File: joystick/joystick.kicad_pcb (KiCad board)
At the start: 2 copper layers, 33 x 34.3 mm, 2 parts, among them J1 Conn_01x04_Male

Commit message: Update joystick breakout board
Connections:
- JS1 pad 4: /V+ -> /GND
- JS1 pad 6: /GND -> /V+
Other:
- board text added: "Joystick Breakout Board Rev. 1 (20200611)"
- board text added: "Maarten De Munck Vijfendertig BVBA"
- board text added: "X→"
- board text added: "Y→"
- board text removed: "Joystick breakout board"
- board text removed: "Maarten De Munck, 2019"
- board text removed: "X->"
- board text removed: "Y->"

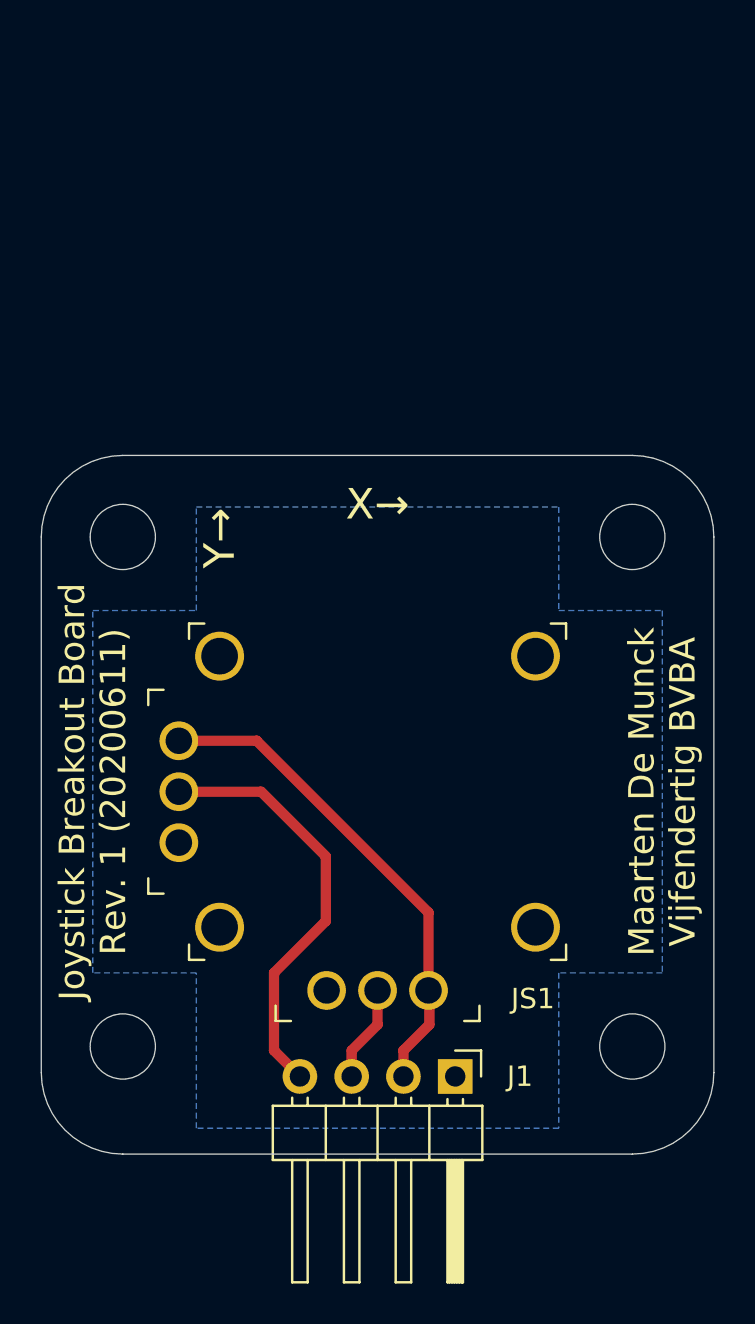
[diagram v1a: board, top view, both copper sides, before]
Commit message: Use proper mounting holes
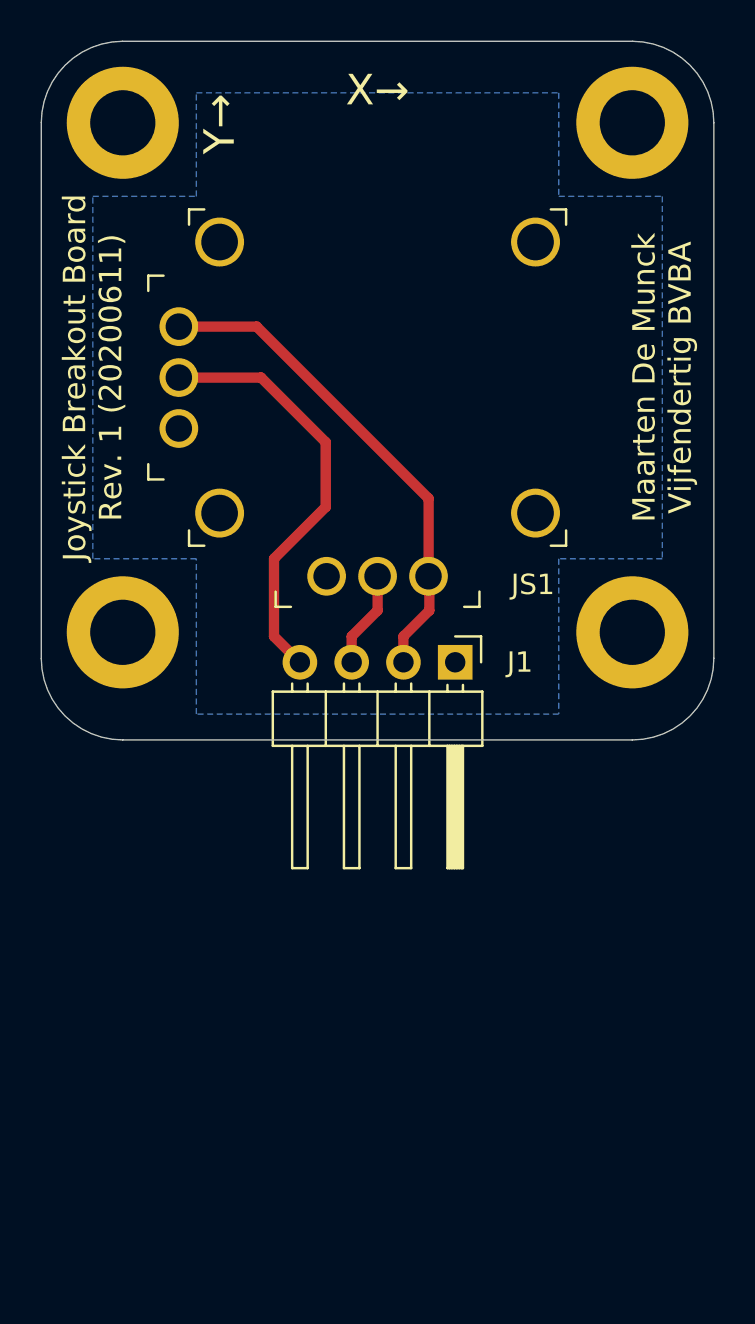
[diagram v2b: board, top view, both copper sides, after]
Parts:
- added REF**: MountingHole_3.2mm_M3_ISO14580_Pad, MountingHole:MountingHole_3.2mm_M3_ISO14580_Pad, F.Cu at (124.3, 149.7)
- added REF**: MountingHole_3.2mm_M3_ISO14580_Pad, MountingHole:MountingHole_3.2mm_M3_ISO14580_Pad, F.Cu at (99.3, 149.7)
- added REF**: MountingHole_3.2mm_M3_ISO14580_Pad, MountingHole:MountingHole_3.2mm_M3_ISO14580_Pad, F.Cu at (99.3, 124.7)
- added REF**: MountingHole_3.2mm_M3_ISO14580_Pad, MountingHole:MountingHole_3.2mm_M3_ISO14580_Pad, F.Cu at (124.3, 124.7)
- moved J1 20.3 mm to (115.6, 151.1)
- moved JS1 20.3 mm to (111.8, 137.2)
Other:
- outline, holes or cut-outs redrawn

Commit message: Update joystick breakout board to KiCad 6.0
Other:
- net class Default removed
- net class Wide removed
